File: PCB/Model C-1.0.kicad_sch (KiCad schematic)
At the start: 70 parts, among them J1 AVR-ISP-6, J1 batt, J2 USB_C_Receptacle_PowerOnly_6P, J4 reset, J5 boot, SW1 SW_SPST, U1 ATmega32A-A, U2 MCP73833-AMI/MF, U3 CA56-12CGKWA, U4 CA56-12CGKWA, U5 MAX7219, U6 MT3608, Y1 Crystal

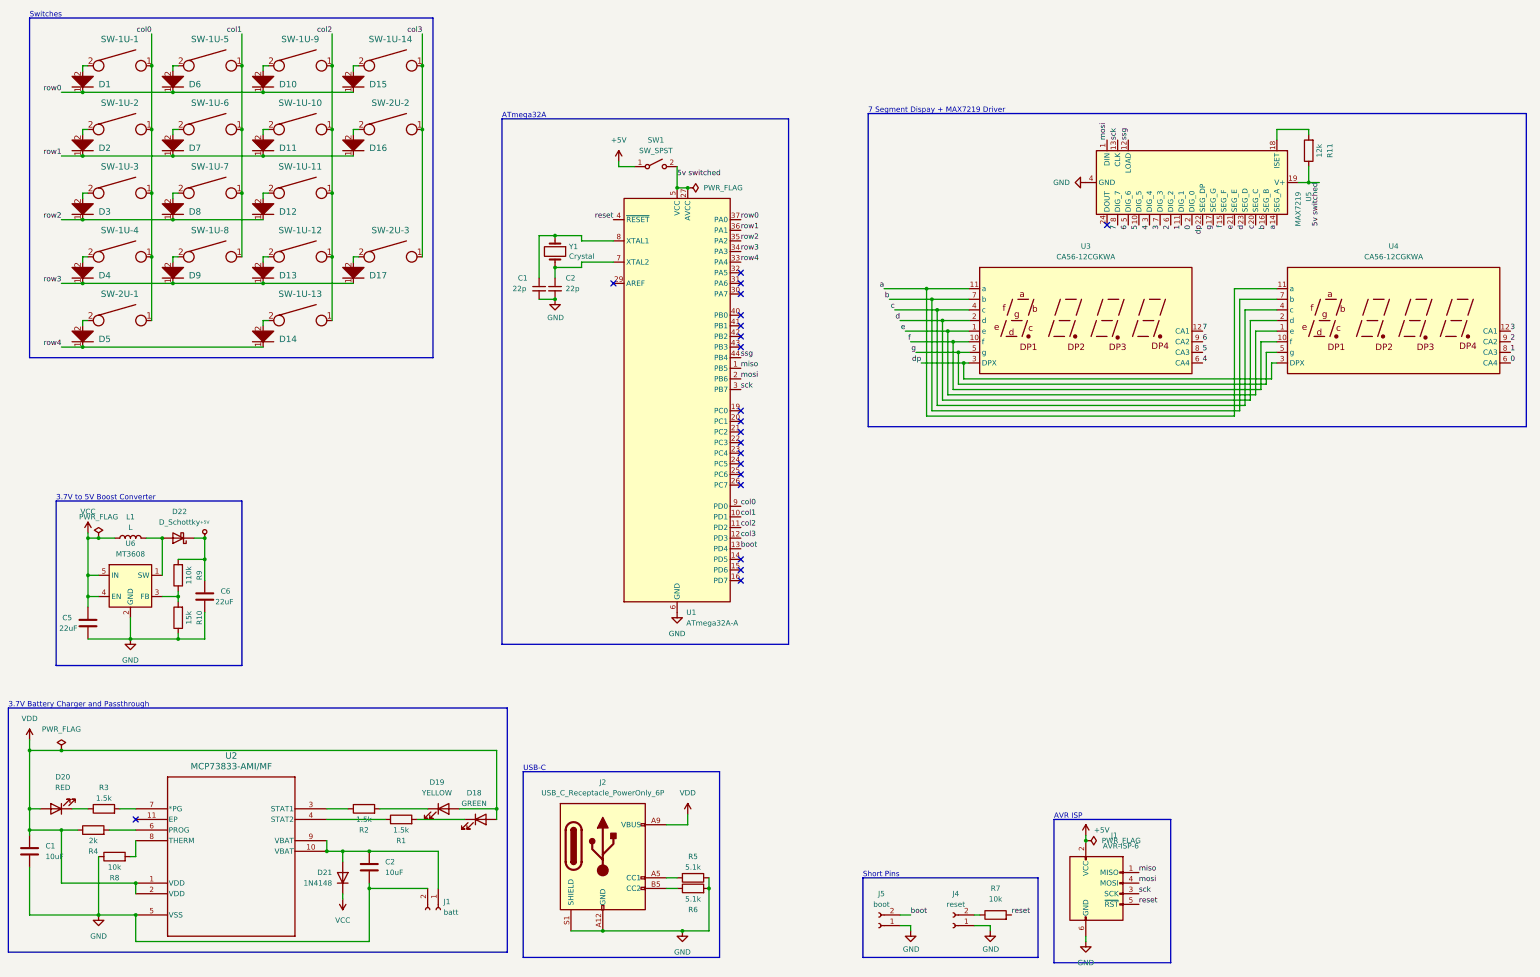
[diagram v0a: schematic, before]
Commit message: swap battery
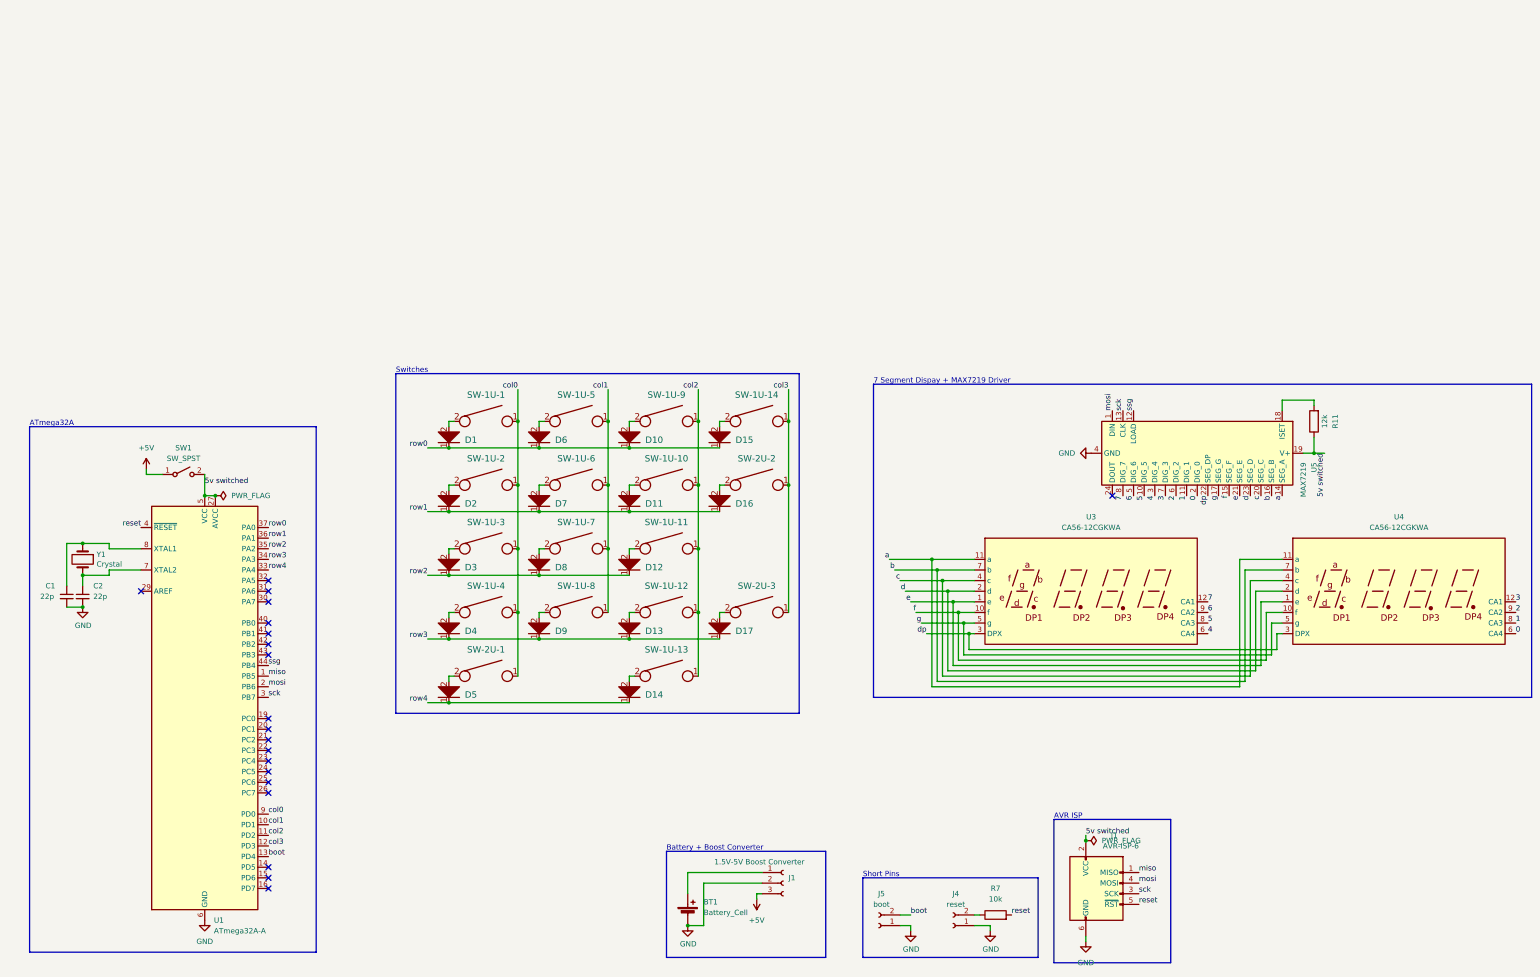
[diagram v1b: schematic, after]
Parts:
- removed C1, C2: 10uF, Capacitor_SMD:C_0805_2012Metric, symbol Device:C
- removed C5, C6: 22uF, Capacitor_SMD:C_0805_2012Metric, symbol Device:C
- removed D18: GREEN, LED_SMD:LED_0805_2012Metric, symbol Device:LED
- removed D19: YELLOW, LED_SMD:LED_0805_2012Metric, symbol Device:LED
- removed D20: RED, LED_SMD:LED_0805_2012Metric, symbol Device:LED
- removed D21: 1N4148, Diode_SMD:D_0805_2012Metric, symbol Device:D
- removed D22: D_Schottky, Diode_SMD:D_0805_2012Metric, symbol Device:D_Schottky
- removed J1: batt, Connector_JST:JST_PH_B2B-PH-K_1x02_P2.00mm_Vertical, symbol Connector:Conn_01x02_Socket
- removed J2: USB_C_Receptacle_PowerOnly_6P, Connector_USB:USB_C_Receptacle_HCTL_HC-TYPE-C-16P-01A, symbol Connector:USB_C_Receptacle_PowerOnly_6P
- removed L1: L, Inductor_SMD:L_0805_2012Metric, symbol Device:L
- removed R1, R2, R3: 1.5k, Resistor_SMD:R_0805_2012Metric, symbol Device:R
- removed R10: 15k, Resistor_SMD:R_0805_2012Metric, symbol Device:R
- removed R4: 2k, Resistor_SMD:R_0805_2012Metric, symbol Device:R
- removed R5, R6: 5.1k, Resistor_SMD:R_0805_2012Metric, symbol Device:R
- removed R8: 10k, Resistor_SMD:R_0805_2012Metric, symbol Device:R
- removed R9: 110k, Resistor_SMD:R_0805_2012Metric, symbol Device:R
- removed U2: MCP73833-AMI/MF, footprints:DFN10_3x3MC_MCH, symbol 2023-10-17_22-34-22:MCP73833-AMI_MF
- removed U6: MT3608, Package_TO_SOT_SMD:SOT-23-6, symbol Regulator_Switching:MT3608
- added BT1: Battery_Cell, Battery:BatteryHolder_Keystone_1058_1x2032, symbol Device:Battery_Cell
- added J1: 1.5V-5V Boost Converter, Connector_JST:JST_PH_B3B-PH-K_1x03_P2.00mm_Vertical, symbol Connector:Conn_01x03_Socket
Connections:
- net +5V: now also J1.3 (Pin_3); no longer J1.2 (VCC)
- net 5v switched: now also J1.2 (VCC)
- net GND: now also BT1.2 (-), J1.2 (Pin_2)
- new net: BT1.1 (+), J1.1 (Pin_1)
- no-connect marks 21 -> 20
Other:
- note added: "Battery + Boost Converter"
- note removed: "3.7V Battery Charger and Passthrough"
- note removed: "3.7V to 5V Boost Converter"
- note removed: "USB-C"
- moved on the sheet: C1, C2, D1, D10, D11, D12, D13, D14, D15, D16, D17, D2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

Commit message: better pcb with the right components - maybe final?
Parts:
- BT1: footprint Battery:BatteryHolder_Keystone_1058_1x2032 -> Battery:BatteryHolder_Keystone_2466_1xAAA
- SW1: footprint Button_Switch_SMD:SW_SPST_TL3305A -> Button_Switch_THT:SW_CuK_OS102011MA1QN1_SPDT_Angled
- U5: footprint Package_DIP:DIP-24_W7.62mm_SMDSocket_SmallPads -> Package_SO:SSOP-24_3.9x8.7mm_P0.635mm
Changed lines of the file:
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@@
       (effects (font (size 1.27 1.27)))
     )
-    (property "Footprint" "Button_Switch_SMD:SW_SPST_TL3305A" (at 59.69 165.1 0)
+    (property "Footprint" "Button_Switch_THT:SW_CuK_OS102011MA1QN1_SPDT_Angled" (at 59.69 165.1 0)
       (effects (font (size 1.27 1.27)) hide)
     )
@@
       (effects (font (size 1.27 1.27)) (justify left))
     )
-    (property "Footprint" "Package_DIP:DIP-24_W7.62mm_SMDSocket_SmallPads" (at 303.53 158.75 0)
+    (property "Footprint" "Package_SO:SSOP-24_3.9x8.7mm_P0.635mm" (at 303.53 158.75 0)
       (effects (font (size 1.27 1.27)) hide)
     )
@@
       (effects (font (size 1.27 1.27)) (justify left))
     )
-    (property "Footprint" "Battery:BatteryHolder_Keystone_1058_1x2032" (at 180.34 268.986 90)
-      (effects (font (size 1.27 1.27)) hide)
-    )
+    (property "Footprint" "Battery:BatteryHolder_Keystone_2466_1xAAA" (at 180.34 268.986 90)
+      (effects (font (size 1.27 1.27)) hide)
+    )

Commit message: mounting holes + clean drc
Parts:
- added H1, H2, H3, H4, H5, H6, H7, H8, H9: MountingHole, MountingHole:MountingHole_3.2mm_M3, symbol Mechanical:MountingHole
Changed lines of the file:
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@@
+    )
+  )
+  (symbol (lib_id "Mechanical:MountingHole") (at 105.41 252.73 0) (unit 1)
+    (in_bom yes) (on_board yes) (dnp no) (fields_autoplaced)
+    (property "Reference" "H3" (at 107.95 251.46 0)
+      (effects (font (size 1.27 1.27)) (justify left))
+    )
+    (property "Value" "MountingHole" (at 107.95 254 0)
+      (effects (font (size 1.27 1.27)) (justify left))
+    )
+    (property "Footprint" "MountingHole:MountingHole_3.2mm_M3" (at 105.41 252.73 0)
+      (effects (font (size 1.27 1.27)) hide)
+    )
+    (property "Datasheet" "~" (at 105.41 252.73 0)
+      (effects (font (size 1.27 1.27)) hide)
+    )
+    (instances
+      (project "Model C-1.0"
+        (path "/0b784d31-5e40-45f3-acfe-8b27f4fc25f5"
+          (reference "H3") (unit 1)
+        )
+      )
     )
   )
@@
         (path "/e63e39d7-6ac0-4ffd-8aa3-1841a4541b55"
           (reference "SW-1U-5") (unit 1)
+        )
+      )
+    )
+  )
+  (symbol (lib_id "Mechanical:MountingHole") (at 105.41 267.97 0) (unit 1)
+    (in_bom yes) (on_board yes) (dnp no) (fields_autoplaced)
+    (property "Reference" "H5" (at 107.95 266.7 0)
+      (effects (font (size 1.27 1.27)) (justify left))
+    )
+    (property "Value" "MountingHole" (at 107.95 269.24 0)
+      (effects (font (size 1.27 1.27)) (justify left))
+    )
+    (property "Footprint" "MountingHole:MountingHole_3.2mm_M3" (at 105.41 267.97 0)
+      (effects (font (size 1.27 1.27)) hide)
+    )
+    (property "Datasheet" "~" (at 105.41 267.97 0)
+      (effects (font (size 1.27 1.27)) hide)
+    )
+    (instances
+      (project "Model C-1.0"
+        (path "/0b784d31-5e40-45f3-acfe-8b27f4fc25f5"
+          (reference "H5") (unit 1)
         )
       )
@@
         (path "/e63e39d7-6ac0-4ffd-8aa3-1841a4541b55"
           (reference "SW-1U-15") (unit 1)
+        )
+      )
+    )
+  )
+  (symbol (lib_id "Mechanical:MountingHole") (at 105.41 275.59 0) (unit 1)
+    (in_bom yes) (on_board yes) (dnp no) (fields_autoplaced)
+    (property "Reference" "H6" (at 107.95 274.32 0)
+      (effects (font (size 1.27 1.27)) (justify left))
+    )
+    (property "Value" "MountingHole" (at 107.95 276.86 0)
+      (effects (font (size 1.27 1.27)) (justify left))
+    )
+    (property "Footprint" "MountingHole:MountingHole_3.2mm_M3" (at 105.41 275.59 0)
+      (effects (font (size 1.27 1.27)) hide)
+    )
+    (property "Datasheet" "~" (at 105.41 275.59 0)
+      (effects (font (size 1.27 1.27)) hide)
+    )
+    (instances
+      (project "Model C-1.0"
+        (path "/0b784d31-5e40-45f3-acfe-8b27f4fc25f5"
+          (reference "H6") (unit 1)
         )
       )
@@
     )
   )
+  (symbol (lib_id "Mechanical:MountingHole") (at 125.73 243.84 0) (unit 1)
+    (in_bom yes) (on_board yes) (dnp no) (fields_autoplaced)
+    (property "Reference" "H7" (at 128.27 242.57 0)
+      (effects (font (size 1.27 1.27)) (justify left))
+    )
+    (property "Value" "MountingHole" (at 128.27 245.11 0)
+      (effects (font (size 1.27 1.27)) (justify left))
+    )
+    (property "Footprint" "MountingHole:MountingHole_3.2mm_M3" (at 125.73 243.84 0)
+      (effects (font (size 1.27 1.27)) hide)
+    )
+    (property "Datasheet" "~" (at 125.73 243.84 0)
+      (effects (font (size 1.27 1.27)) hide)
+    )
+    (instances
+      (project "Model C-1.0"
+        (path "/0b784d31-5e40-45f3-acfe-8b27f4fc25f5"
+          (reference "H7") (unit 1)
+        )
+      )
+    )
+  )
   (symbol (lib_id "Device:R") (at 254 270.51 90) (unit 1)
     (in_bom yes) (on_board yes) (dnp no) (fields_autoplaced)
@@
         (path "/e63e39d7-6ac0-4ffd-8aa3-1841a4541b55"
           (reference "SW-1U-4") (unit 1)
+        )
+      )
+    )
+  )
+  (symbol (lib_id "Mechanical:MountingHole") (at 105.41 260.35 0) (unit 1)
+    (in_bom yes) (on_board yes) (dnp no) (fields_autoplaced)
+    (property "Reference" "H4" (at 107.95 259.08 0)
+      (effects (font (size 1.27 1.27)) (justify left))
+    )
+    (property "Value" "MountingHole" (at 107.95 261.62 0)
+      (effects (font (size 1.27 1.27)) (justify left))
+    )
+    (property "Footprint" "MountingHole:MountingHole_3.2mm_M3" (at 105.41 260.35 0)
+      (effects (font (size 1.27 1.27)) hide)
+    )
+    (property "Datasheet" "~" (at 105.41 260.35 0)
+      (effects (font (size 1.27 1.27)) hide)
+    )
+    (instances
+      (project "Model C-1.0"
+        (path "/0b784d31-5e40-45f3-acfe-8b27f4fc25f5"
+          (reference "H4") (unit 1)
         )
       )
@@
     )
   )
+  (symbol (lib_id "Mechanical:MountingHole") (at 105.41 240.03 0) (unit 1)
+    (in_bom yes) (on_board yes) (dnp no) (fields_autoplaced)
+    (property "Reference" "H1" (at 107.95 238.76 0)
+      (effects (font (size 1.27 1.27)) (justify left))
+    )
+    (property "Value" "MountingHole" (at 107.95 241.3 0)
+      (effects (font (size 1.27 1.27)) (justify left))
+    )
+    (property "Footprint" "MountingHole:MountingHole_3.2mm_M3" (at 105.41 240.03 0)
+      (effects (font (size 1.27 1.27)) hide)
+    )
+    (property "Datasheet" "~" (at 105.41 240.03 0)
+      (effects (font (size 1.27 1.27)) hide)
+    )
+    (instances
+      (project "Model C-1.0"
+        (path "/0b784d31-5e40-45f3-acfe-8b27f4fc25f5"
+          (reference "H1") (unit 1)
+        )
+      )
+    )
+  )
   (symbol (lib_id "keyboard_parts:KEYSW") (at 196.85 198.12 0) (unit 1)
     (in_bom yes) (on_board yes) (dnp no) (fields_autoplaced)
@@
     )
   )
+  (symbol (lib_id "Mechanical:MountingHole") (at 105.41 246.38 0) (unit 1)
+    (in_bom yes) (on_board yes) (dnp no) (fields_autoplaced)
+    (property "Reference" "H2" (at 107.95 245.11 0)
+      (effects (font (size 1.27 1.27)) (justify left))
+    )
+    (property "Value" "MountingHole" (at 107.95 247.65 0)
+      (effects (font (size 1.27 1.27)) (justify left))
+    )
+    (property "Footprint" "MountingHole:MountingHole_3.2mm_M3" (at 105.41 246.38 0)
+      (effects (font (size 1.27 1.27)) hide)
+    )
+    (property "Datasheet" "~" (at 105.41 246.38 0)
+      (effects (font (size 1.27 1.27)) hide)
+    )
+    (instances
+      (project "Model C-1.0"
+        (path "/0b784d31-5e40-45f3-acfe-8b27f4fc25f5"
+          (reference "H2") (unit 1)
+        )
+      )
+    )
+  )
   (symbol (lib_id "keyboard_parts:D") (at 166.37 157.48 180) (unit 1)
     (in_bom yes) (on_board yes) (dnp no) (fields_autoplaced)
@@
         (path "/0b784d31-5e40-45f3-acfe-8b27f4fc25f5"
           (reference "#FLG04") (unit 1)
+        )
+      )
+    )
+  )
+  (symbol (lib_id "Mechanical:MountingHole") (at 125.73 250.19 0) (unit 1)
+    (in_bom yes) (on_board yes) (dnp no) (fields_autoplaced)
+    (property "Reference" "H8" (at 128.27 248.92 0)
+      (effects (font (size 1.27 1.27)) (justify left))
+    )
+    (property "Value" "MountingHole" (at 128.27 251.46 0)
+      (effects (font (size 1.27 1.27)) (justify left))
+    )
+    (property "Footprint" "MountingHole:MountingHole_3.2mm_M3" (at 125.73 250.19 0)
+      (effects (font (size 1.27 1.27)) hide)
+    )
+    (property "Datasheet" "~" (at 125.73 250.19 0)
+      (effects (font (size 1.27 1.27)) hide)
+    )
+    (instances
+      (project "Model C-1.0"
+        (path "/0b784d31-5e40-45f3-acfe-8b27f4fc25f5"
+          (reference "H8") (unit 1)
         )
       )
@@
         )
       )
+    )
+  )
+  (symbol (lib_id "Mechanical:MountingHole") (at 125.73 257.81 0) (unit 1)
+    (in_bom yes) (on_board yes) (dnp no) (fields_autoplaced)
+    (property "Reference" "H9" (at 128.27 256.54 0)
+      (effects (font (size 1.27 1.27)) (justify left))
+    )
+    (property "Value" "MountingHole" (at 128.27 259.08 0)
+      (effects (font (size 1.27 1.27)) (justify left))
+    )
+    (property "Footprint" "MountingHole:MountingHole_3.2mm_M3" (at 125.73 257.81 0)
+      (effects (font (size 1.27 1.27)) hide)
+    )
+    (property "Datasheet" "~" (at 125.73 257.81 0)
+      (effects (font (size 1.27 1.27)) hide)
+    )
+    (instances
+      (project "Model C-1.0"
+        (path "/0b784d31-5e40-45f3-acfe-8b27f4fc25f5"
+          (reference "H9") (unit 1)
+        )
+      )
